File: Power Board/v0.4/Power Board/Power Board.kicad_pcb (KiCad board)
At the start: 4 copper layers, 66 x 80 mm, 80 parts, among them J1 Battery In, J2 JST B2PS-VH, J3 JST B2PS-VH, J4 JST B2PS-VH, J5 JST B2PS-VH, J6 JST B2PS-VH, J7 JST B2PS-VH, J8 Molex 70553-0006, J9 Conn_02x05_Odd_Even, Q1 SI5504BDC, SW1 SW_Push, U1 LMZ14203, U2 TPS53819A, U3 CSD86360Q5D

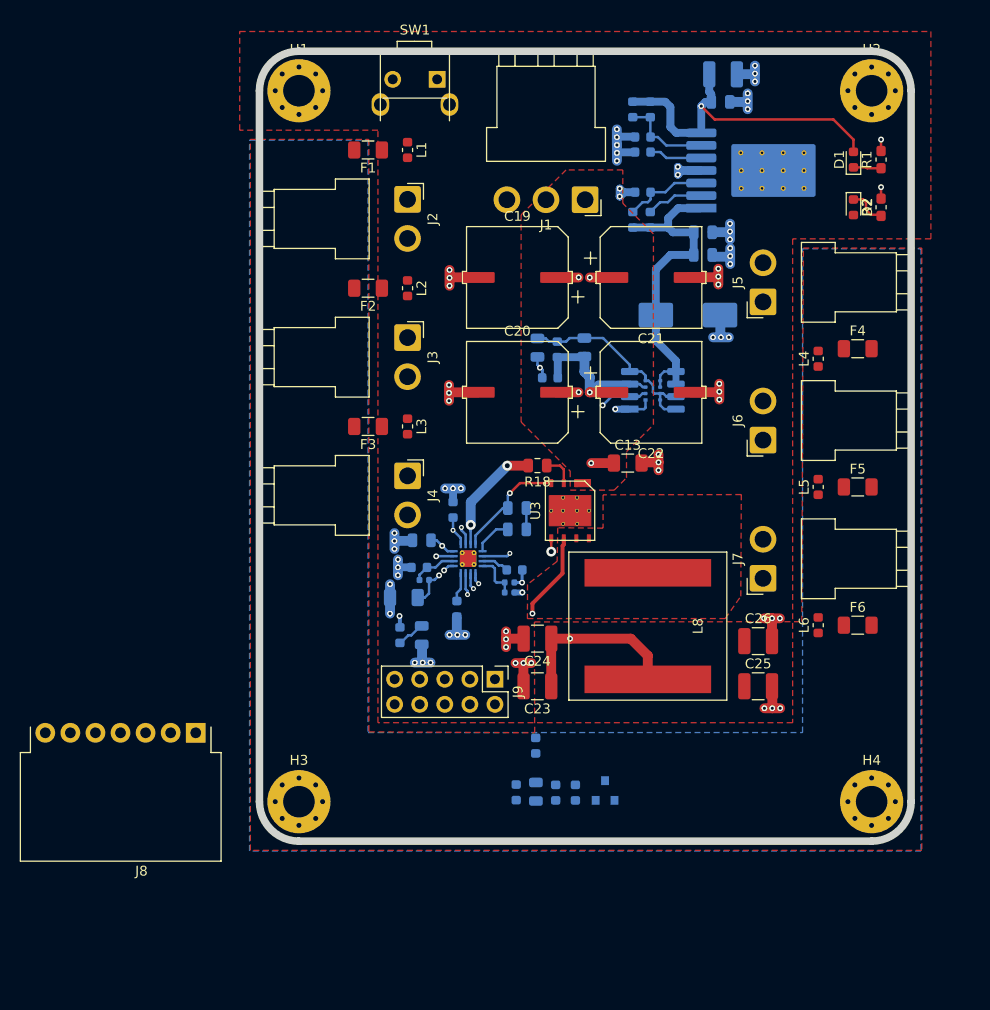
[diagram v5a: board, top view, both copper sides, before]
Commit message: Widen board to 70mm, delineate mechanical keepout zones.
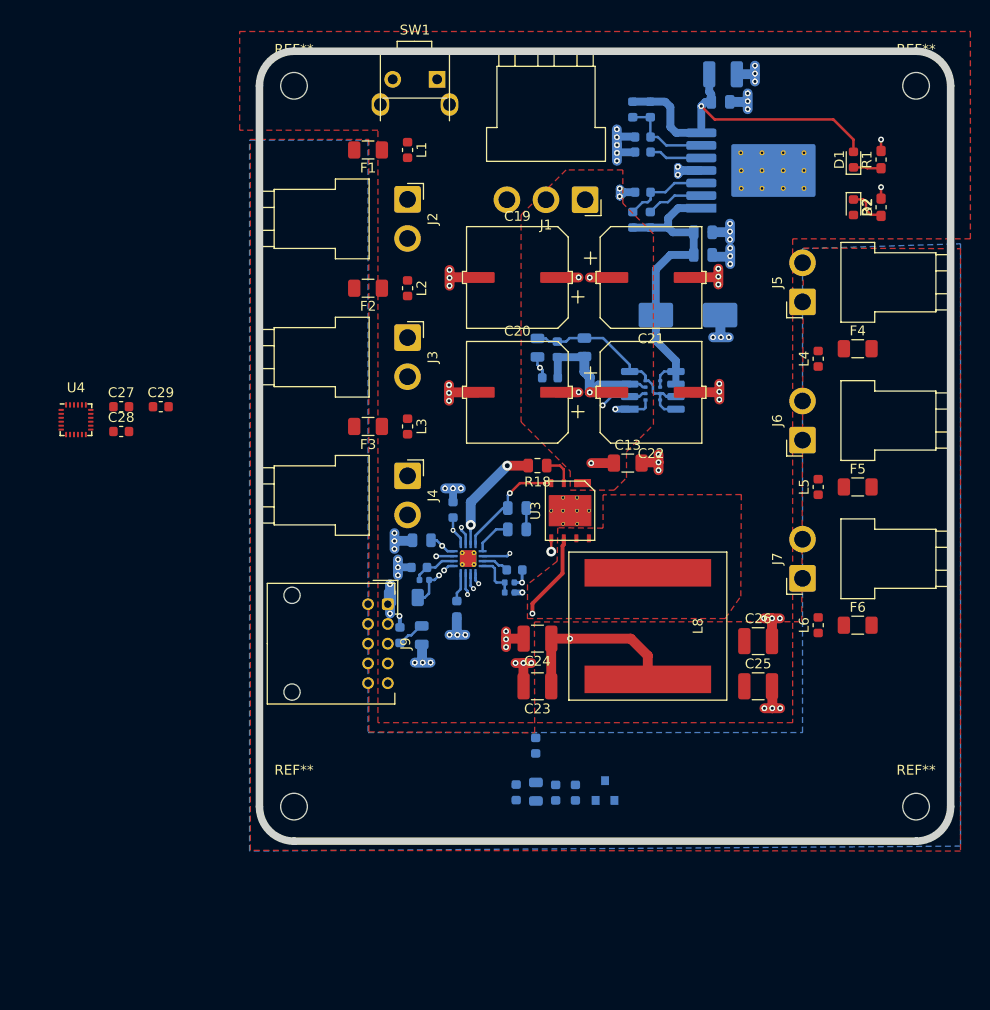
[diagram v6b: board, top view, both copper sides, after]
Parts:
- removed H1, H2, H3, H4: M3, MountingHole:MountingHole_3.2mm_M3_Pad_Via
- removed J8: Molex 70553-0006, Power_Board:Molex_SL_70553-0006
- added C27: 100nF, Capacitor_SMD:C_0603_1608Metric, F.Cu at (63.0, 71.0)
- added C28: 100nF, Capacitor_SMD:C_0603_1608Metric, F.Cu at (63.0, 73.5)
- added C29: 10nF, Capacitor_SMD:C_0603_1608Metric, F.Cu at (67.0, 71.0)
- added REF**: MountingHole_2.7mm_M2.5, MountingHole:MountingHole_2.7mm_M2.5, F.Cu at (80.5, 111.5)
- added REF**: MountingHole_2.7mm_M2.5, MountingHole:MountingHole_2.7mm_M2.5, F.Cu at (143.5, 111.5)
- added REF**: MountingHole_2.7mm_M2.5, MountingHole:MountingHole_2.7mm_M2.5, F.Cu at (143.5, 38.5)
- added REF**: MountingHole_2.7mm_M2.5, MountingHole:MountingHole_2.7mm_M2.5, F.Cu at (80.5, 38.5)
- added U4: MPU-9250, Sensor_Motion:InvenSense_QFN-24_3x3mm_P0.4mm, F.Cu at (58.4, 72.3)
- J9: value Conn_02x05_Odd_Even -> Raspberry Pi; footprint Connector_PinHeader_2.54mm:PinHeader_2x05_P2.54mm_Vertical -> Connector_JST:JST_PUD_S10B-PUDSS-1_2x05_P2.00mm_Horizontal
- moved J9 13.2 mm to (90.0, 91.0)
- moved J5 4.00 mm to (132.0, 60.4)
- moved J6 4.00 mm to (132.0, 74.4)
- moved J7 4.00 mm to (132.0, 88.4)
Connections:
- J9 pad 1: Net-(J9-Pad1) -> Pi_3.3V
- J9 pad 10: Net-(J9-Pad10) -> /Power_Sense
- J9 pad 2: Net-(J9-Pad2) -> /+5.2V
- J9 pad 3: Net-(J9-Pad3) -> SDA
- J9 pad 4: Net-(J9-Pad4) -> /+5.2V
- J9 pad 5: Net-(J9-Pad5) -> SCL
- J9 pad 6: Net-(J9-Pad6) -> GND
- J9 pad 7: Net-(J9-Pad7) -> /Panel_Alert
- J9 pad 8: Net-(J9-Pad8) -> /Power_Ctl
- J9 pad 9: Net-(J9-Pad9) -> GND
- U2 pad 1: /SCL -> SCL
- U2 pad 2: /SDA -> SDA
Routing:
- net SDA: track 0.00 -> 1.70 mm, vias 0 -> 1
- net /SDA: track 1.70 -> 0.00 mm, vias 1 -> 0
- net SCL: track 0.00 -> 1.21 mm, vias 0 -> 1
- net /SCL: track 1.21 -> 0.00 mm, vias 1 -> 0
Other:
- board size 66 x 80 mm -> 70 x 80 mm
- board text added: "No components over 5mm tall on back in this region"

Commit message: Almost Rough Draft Done
Mostly routed but needs lots of TLC. Need to check rule definitions before DRC
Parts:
- removed REF** (x4): MountingHole_2.7mm_M2.5, MountingHole:MountingHole_2.7mm_M2.5
- added C30: 100nF, Capacitor_SMD:C_0603_1608Metric, B.Cu at (94.0, 45.2)
- added R22: 100K 1%, Resistor_SMD:R_0603_1608Metric, B.Cu at (97.8, 48.8)
- added R23: 17.8K 1%, Resistor_SMD:R_0603_1608Metric, B.Cu at (96.0, 48.8)
- added R24: 100k, Resistor_SMD:R_0603_1608Metric, B.Cu at (101.9, 86.0)
- added U5: ADS1000, Package_TO_SOT_SMD:SOT-23-6, B.Cu at (93.2, 48.3)
- C27, C28, C29, U4: moved to B.Cu
- C5, D3, R5, R6, R7: moved to F.Cu
- L1, L2, L3, L4, L5, L6: value 70R -> 60R; footprint Inductor_SMD:L_0603_1608Metric -> Inductor_SMD:L_1206_3216Metric
- moved C5 68.6 mm to (84.8, 44.5), turned to 180 degrees
- moved R5 66.2 mm to (84.6, 46.5), turned to 0 degrees
- moved R7 65.8 mm to (84.6, 48.3), turned to 180 degrees
- moved R6 64.8 mm to (84.6, 50.0), turned to 180 degrees
- moved L7 64.1 mm to (85.9, 44.2), turned to 270 degrees
- moved D3 63.4 mm to (84.3, 52.8), turned to 180 degrees
- moved J9 45.3 mm to (89.7, 45.7)
- moved U4 40.5 mm to (93.9, 52.8), turned to 270 degrees
- moved C28 39.3 mm to (97.0, 53.8), turned to 270 degrees
- moved C29 36.5 mm to (97.8, 51.3)
- moved C27 34.4 mm to (94.0, 56.1), turned to 180 degrees
- moved F3 18.8 mm to (84.6, 91.4)
- moved L3 18.6 mm to (90.7, 91.6), turned to 0 degrees
- moved J4 17.8 mm to (92.0, 95.8)
- moved F2 13.2 mm to (84.7, 71.8)
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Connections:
- net /Pi Power/Vin_switched renamed Vin_switched
- U2 pad 14: /5.2V_switched -> /Panel Power/Enable
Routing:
- net /5.2V_switched: track 37.2 -> 142.8 mm, vias 2 -> 4
- net SDA: track 1.70 -> 77.1 mm, vias 1 -> 2
- net SCL: track 1.21 -> 71.5 mm
- net /Pi Power/Power_Button: track 2.89 -> 67.5 mm
- net Net-(C5-Pad1): track 4.84 -> 60.9 mm, vias 1 -> 2
- net /Panel_Alert: track 2.25 -> 57.7 mm
- net Pi_3.3V: track 0.00 -> 34.3 mm, vias 0 -> 3
- net Vin_switched: track 33.2 -> 59.8 mm, vias 0 -> 2
- net GND: track 93.8 -> 109.0 mm, vias 73 -> 79
- net /Panel Power/Switch_Node: track 23.9 -> 14.7 mm
- net /Power_Ctl: track 0.00 -> 5.43 mm
- net Net-(R22-Pad2): track 0.00 -> 4.80 mm
- net Net-(R5-Pad1): track 0.00 -> 4.56 mm
- net Net-(J2-Pad1): track 0.00 -> 4.43 mm
- net Net-(J5-Pad1): track 0.00 -> 4.28 mm
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- added copper zone on B.Cu, net GND
- added copper zone on In2.Cu, net GND

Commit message: More routing and zone placements. Needs more TLC Needs DRC review and fix
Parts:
- C5, D3, R5, R6, R7: moved to B.Cu
- L7: value 70R -> 60R; footprint Inductor_SMD:L_0603_1608Metric -> Inductor_SMD:L_1206_3216Metric
- moved L7 2.77 mm to (88.5, 43.4), turned to 180 degrees
- moved C5 2.62 mm to (83.8, 46.9), turned to 0 degrees
- moved R5 2.47 mm to (84.1, 48.9), turned to 180 degrees
- moved R6 2.47 mm to (84.1, 52.5), turned to 0 degrees
- moved R7 2.47 mm to (84.1, 50.7), turned to 0 degrees
- moved D3 2.41 mm to (84.3, 55.2), turned to 0 degrees
- moved R3 1.53 mm to (112.1, 72.9)
- moved C1 1.14 mm to (110.9, 69.6)
- moved R4 1.14 mm to (112.9, 69.8)
- moved C13 0.51 mm to (113.3, 77.9)
- moved C17 0.51 mm to (90.6, 90.8)
- moved C2 0.38 mm to (114.9, 69.6)
- moved R20 0.25 mm to (92.7, 88.8)
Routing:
- net /5.2V_switched: track 142.8 -> 136.5 mm
- net /Pi Power/Power_Button: track 67.5 -> 73.0 mm, vias 1 -> 2
- net Net-(C5-Pad1): track 60.9 -> 65.3 mm
- net /Power_Sense: track 2.36 -> 6.62 mm
- net /Battery_Power: track 47.8 -> 45.9 mm, vias 6 -> 8
- net Net-(C1-Pad1): track 23.0 -> 21.5 mm
- net Vin_switched: track 59.8 -> 58.3 mm
- net /+5.2V: track 4.12 -> 5.55 mm
- net SDA: track 77.1 -> 78.1 mm
- net /Power_Ctl: track 5.43 -> 6.36 mm
- net SCL: track 71.5 -> 70.7 mm
- net Net-(R20-Pad2): track 5.08 -> 4.55 mm
- net GND: track 109.0 -> 108.8 mm, vias 79 -> 76
- added copper zone on B.Cu, net /+5.2V
- added copper zone on B.Cu, net /5.2V_switched
- added copper zone on F.Cu, net Net-(J2-Pad1)
- added copper zone on F.Cu, net Net-(J3-Pad1)
- added copper zone on F.Cu, net Net-(J4-Pad1)
- added copper zone on F.Cu, net Net-(J5-Pad1)
- added copper zone on F.Cu, net Net-(J6-Pad1)
- added copper zone on F.Cu, net Net-(J7-Pad1)
- added copper zone on B.Cu, net Vin_switched
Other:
- net class U2 added: clearance 0.1524, trace_width 0.2, via_dia 0.6, via_drill 0.3
